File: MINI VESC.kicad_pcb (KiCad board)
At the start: 4 copper layers, 65 x 18 mm, 151 parts, among them P1 CONN_1, P10 CONN_01X06, P11 CONN_01X06, P2 CONN_1, P3 CONN_1, P4 CONN_1, P5 CONN_1, P6 CONN_1, P9 CONN_01X06, Q1 Q_NMOS_GSD, Q2 Q_NMOS_GSD, Q3 Q_NMOS_GSD, Q4 Q_NMOS_GSD, Q5 Q_NMOS_GSD, Q6 Q_NMOS_GSD, U1 LM5113, U10 MCP1700, U2 LM5113, U3 LM5113, U4 AD8418, U5 AD8418, U6 AD8418, U7 STM32F40X_LQFP64, U8 LMR16006, U9 MCP1700, X1 CRYSTAL_SMD

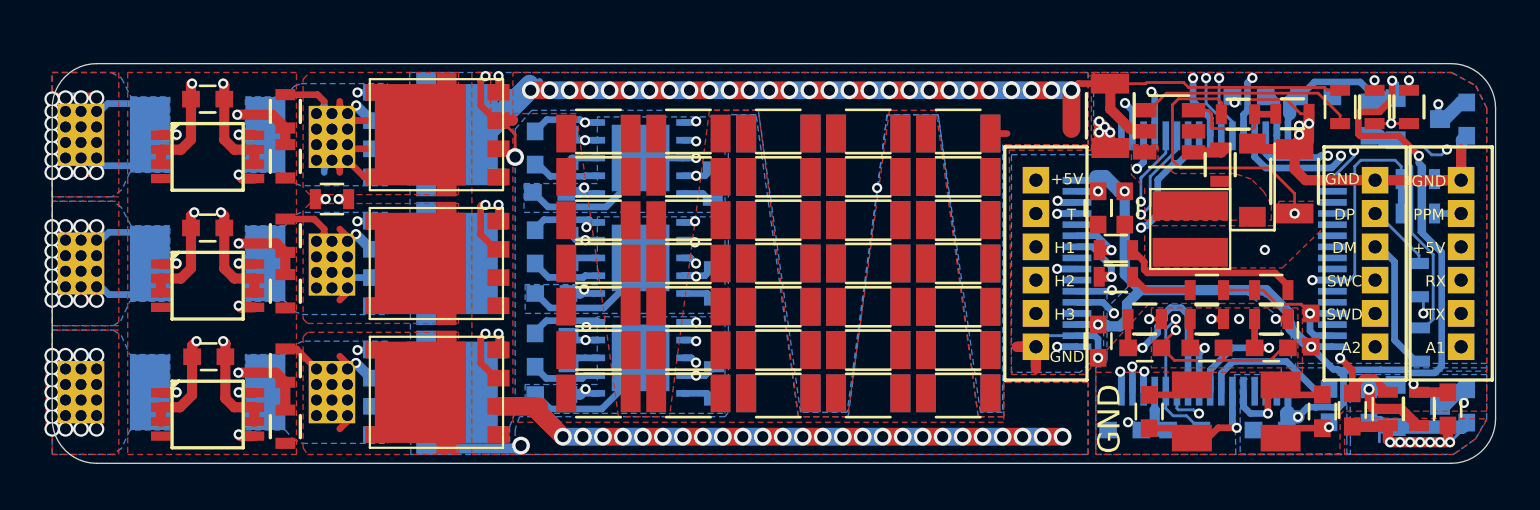
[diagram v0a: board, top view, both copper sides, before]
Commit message: Migrating to KiCAD 7
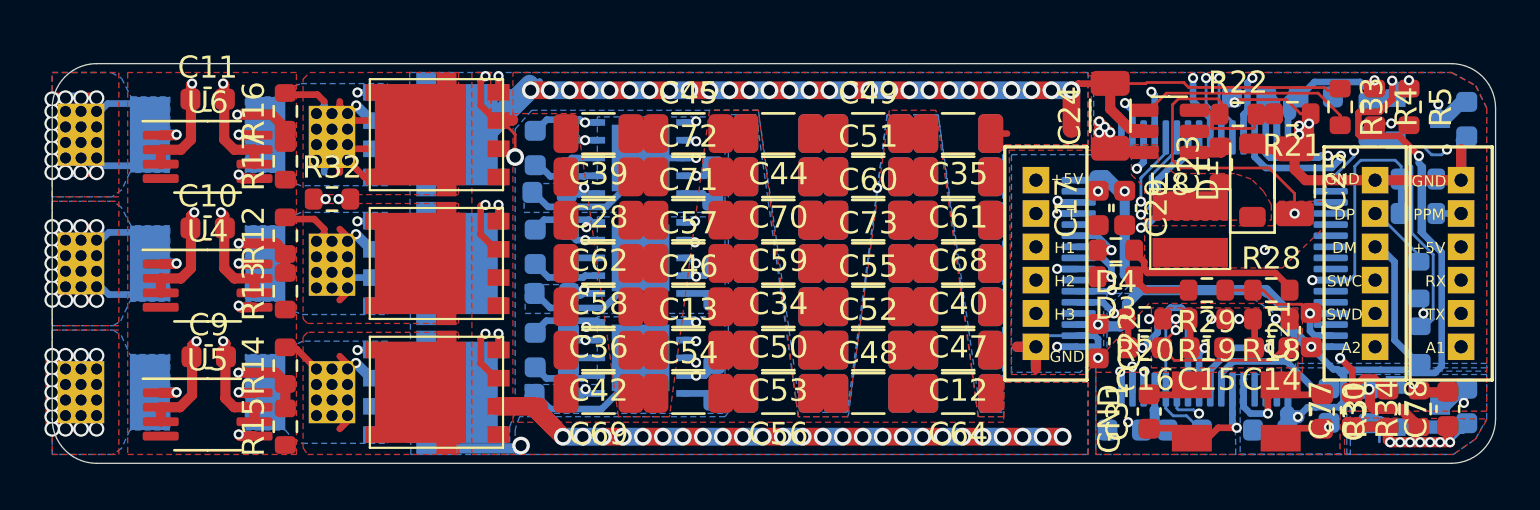
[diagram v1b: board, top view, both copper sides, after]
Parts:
- C1, C10, C11, C14, C15, C16, C17, C18, C19, C2, C20, C21, C22, C26, C27, C29, C3, C30, C31, C6, C7, C77, C78, C8, C86, C87, C88, C89, C9, C90: footprint Capacitors_SMD:C_0603 -> Capacitor_SMD:C_0603_1608Metric
- C12, C13, C24, C25, C28, C32, C33, C34, C35, C36, C37, C38, C39, C4, C40, C41, C42, C43, C44, C45, C46, C47, C48, C49, C5, C50, C51, C52, C53, C54, C55, C56, C57, C58, C59, C60, C61, C62, C63, C64, C65, C66, C67, C68, C69, C70, C71, C72, C73, C74, C75, C79, C80, C81, C82, C83, C84, C85: footprint Resistors_SMD:R_1206 -> Resistor_SMD:R_1206_3216Metric
- C23, C76, D3, D4, R10, R11, R12, R13, R14, R15, R16, R17, R18, R19, R20, R21, R22, R25, R27, R28, R29, R30, R31, R32, R33, R34, R4, R5, R6, R7, R8, R9: footprint Resistors_SMD:R_0603 -> Resistor_SMD:R_0603_1608Metric
- D1: footprint Diodes_SMD:D_SOD-123 -> Diode_SMD:D_SOD-123
- U4, U5, U6: footprint kicad_subory:MSOP -> Package_SO:MSOP-8_3x3mm_P0.65mm
- U7: footprint crf1:lqfp64_pad_mod -> Package_QFP:LQFP-64_10x10mm_P0.5mm
- U8: footprint TO_SOT_Packages_SMD:SOT-23-6 -> Package_TO_SOT_SMD:SOT-23-6
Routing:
- net VSS: track 317.9 -> 335.3 mm
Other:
- net class Default removed

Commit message: Lots of stuff
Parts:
- C1, C2, C3: value 220n -> 470n
- C12, C13, C25, C28, C32, C33, C34, C35, C36, C37, C38, C39, C4, C40, C41, C42, C43, C44, C45, C46, C47, C48, C49, C5, C50, C51, C52, C53, C54, C55, C56, C57, C58, C59, C60, C61, C62, C63, C64, C65, C66, C67, C68, C69, C70, C71, C72, C73, C74, C75, C79, C81, C82, C83, C84, C85: footprint Resistor_SMD:R_1206_3216Metric -> Capacitor_SMD:C_1206_3216Metric
- C19, C21, C22, C26, C27, C29: value 2u2 -> 100n
- C20: value 220nF -> 100n
- C23, C76: footprint Resistor_SMD:R_0603_1608Metric -> Capacitor_SMD:C_0603_1608Metric
- C24: value 10u -> 2u2; footprint Resistor_SMD:R_1206_3216Metric -> Capacitor_SMD:C_1206_3216Metric
- C80: value C -> 10u; footprint Resistor_SMD:R_1206_3216Metric -> Capacitor_SMD:C_1206_3216Metric
- D3, D4: footprint Resistor_SMD:R_0603_1608Metric -> LED_SMD:LED_0603_1608Metric
- L1: value 22uH -> Wurth Electronics 74438335220
- Q1, Q2, Q3, Q4, Q5, Q6: value Q_NMOS_GSD -> NTMFS5C604NLT1G
- R1, R2, R3: value RSENS -> R0005
- R10, R11, R6, R7, R8, R9: value 7R5 -> 3R9
- R12, R14, R4: value 25k5 -> 39k
- R21: value 510R -> 10k
- R22: value 8k -> 54k9
- R33: value 10k -> 100k
- X1: value CRYSTAL_SMD -> ABM3B-8.000MHZ
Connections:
- C1 pad 1: Net-(C1-Pad1) -> Net-(U1-HB)
- C17 pad 2: Net-(C17-Pad2) -> Net-(U7-VCAP1)
- C18 pad 2: Net-(C18-Pad2) -> Net-(U7-VCAP2)
- C2 pad 1: Net-(C2-Pad1) -> Net-(U2-HB)
- C20 pad 2: Net-(C20-Pad2) -> Net-(U7-NRST)
- C23 pad 1: Net-(C23-Pad1) -> Net-(D1-K)
- C23 pad 2: Net-(C23-Pad2) -> Net-(U8-BST)
- C3 pad 1: Net-(C3-Pad1) -> Net-(U3-HB)
- C30 pad 1: Net-(C30-Pad1) -> Net-(U7-PH0-OSC_IN)
- C31 pad 1: Net-(C31-Pad1) -> Net-(U7-PH1-OSC_OUT)
- C77 pad 2: Net-(C77-Pad2) -> Net-(U7-PA3(ADC123_IN3))
- L1 pad 1: Net-(C23-Pad1) -> Net-(D1-K)
- P1 pad 1: Net-(P1-Pad1) -> Net-(U4-IN-)
- P2 pad 1: Net-(P2-Pad1) -> Net-(U5-IN-)
- P3 pad 1: Net-(P3-Pad1) -> Net-(U6-IN-)
- Q1 pad 1: Net-(Q1-Pad1) -> Net-(Q1-G)
- Q2 pad 1: Net-(Q2-Pad1) -> Net-(Q2-G)
- Q3 pad 1: Net-(Q3-Pad1) -> Net-(Q3-G)
- Q4 pad 1: Net-(Q4-Pad1) -> Net-(Q4-G)
- Q5 pad 1: Net-(Q5-Pad1) -> Net-(Q5-G)
- Q6 pad 1: Net-(Q6-Pad1) -> Net-(Q6-G)
- R1 pad 1: Net-(P1-Pad1) -> Net-(U4-IN-)
- R10 pad 1: Net-(Q5-Pad1) -> Net-(Q5-G)
- R10 pad 2: Net-(R10-Pad2) -> Net-(U3-HO)
- R11 pad 1: Net-(R11-Pad1) -> Net-(U3-LO)
- R11 pad 2: Net-(Q6-Pad1) -> Net-(Q6-G)
- R2 pad 1: Net-(P2-Pad1) -> Net-(U5-IN-)
- R21 pad 2: Net-(R21-Pad2) -> Net-(U8-FB)
- R22 pad 2: Net-(R21-Pad2) -> Net-(U8-FB)
- R3 pad 1: Net-(P3-Pad1) -> Net-(U6-IN-)
- R31 pad 2: Net-(C77-Pad2) -> Net-(U7-PA3(ADC123_IN3))
- R32 pad 2: Net-(C77-Pad2) -> Net-(U7-PA3(ADC123_IN3))
- R6 pad 1: Net-(Q1-Pad1) -> Net-(Q1-G)
- R6 pad 2: Net-(R6-Pad2) -> Net-(U1-HO)
- R7 pad 1: Net-(R7-Pad1) -> Net-(U1-LO)
- R7 pad 2: Net-(Q2-Pad1) -> Net-(Q2-G)
- R8 pad 1: Net-(Q3-Pad1) -> Net-(Q3-G)
- R8 pad 2: Net-(R8-Pad2) -> Net-(U2-HO)
- R9 pad 1: Net-(R9-Pad1) -> Net-(U2-LO)
- R9 pad 2: Net-(Q4-Pad1) -> Net-(Q4-G)
- X1 pad 1: Net-(C30-Pad1) -> Net-(U7-PH0-OSC_IN)
- X1 pad 2: Net-(C31-Pad1) -> Net-(U7-PH1-OSC_OUT)
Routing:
- net VDD: track 123.7 -> 105.7 mm
- net VSS: track 335.3 -> 321.1 mm
- net Net-(U5-IN-): track 0.00 -> 11.5 mm, vias 0 -> 13
- net Net-(P2-Pad1): track 13.4 -> 1.92 mm, vias 14 -> 1
- net Net-(D4-Pad1): track 0.00 -> 8.12 mm
- net Net-(D4-K): track 8.12 -> 0.00 mm
- net ADC_EXT2: track 15.3 -> 21.9 mm, vias 1 -> 2
- net Net-(C31-Pad1): track 6.65 -> 0.00 mm, vias 1 -> 0
- net ADC_EXT1: track 35.3 -> 41.7 mm, vias 2 -> 3
- net Net-(C30-Pad1): track 6.43 -> 0.00 mm, vias 1 -> 0
- net Net-(U7-Pad23): track 0.00 -> 6.38 mm
- net Net-(C20-Pad2): track 6.38 -> 0.00 mm
- net Net-(P10-Pin_4): track 6.22 -> 0.00 mm
- net (no net): track 0.00 -> 6.22 mm
- net VCC: track 86.4 -> 82.9 mm
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- added copper zone on F.Cu, net Net-(D1-K)
- added copper zone on B.Cu, net Net-(U4-IN-)
- added copper zone on F.Cu, net Net-(U4-IN-)
- added copper zone on In1.Cu, net Net-(U4-IN-)
- added copper zone on In2.Cu, net Net-(U4-IN-)
- added copper zone on B.Cu, net Net-(U5-IN-)
- added copper zone on F.Cu, net Net-(U5-IN-)
- added copper zone on In1.Cu, net Net-(U5-IN-)
- added copper zone on In2.Cu, net Net-(U5-IN-)
- added copper zone on B.Cu, net Net-(U6-IN-)
- added copper zone on F.Cu, net Net-(U6-IN-)
- added copper zone on In1.Cu, net Net-(U6-IN-)
- added copper zone on In2.Cu, net Net-(U6-IN-)
- removed copper zone on F.Cu, net Net-(C23-Pad1)
- removed copper zone on B.Cu, net Net-(P1-Pad1)
- removed copper zone on F.Cu, net Net-(P1-Pad1)
- removed copper zone on In1.Cu, net Net-(P1-Pad1)
- removed copper zone on In2.Cu, net Net-(P1-Pad1)
- removed copper zone on B.Cu, net Net-(P2-Pad1)
- removed copper zone on F.Cu, net Net-(P2-Pad1)
- removed copper zone on In1.Cu, net Net-(P2-Pad1)
- removed copper zone on In2.Cu, net Net-(P2-Pad1)
- removed copper zone on B.Cu, net Net-(P3-Pad1)
- removed copper zone on F.Cu, net Net-(P3-Pad1)
- removed copper zone on In1.Cu, net Net-(P3-Pad1)
- removed copper zone on In2.Cu, net Net-(P3-Pad1)

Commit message: More work
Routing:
- net VSS: track 321.1 -> 298.6 mm
- net VDD: track 105.7 -> 93.0 mm
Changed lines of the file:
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@@
   (segment (start 132.52 85.07) (end 130.85 83.4) (width 0.127) (layer "In1.Cu") (net 1))
   (segment (start 88.2825 83.295) (end 89.455 83.295) (width 0.3) (layer "B.Cu") (net 1))
-  (segment (start 92.2 83.2) (end 93.1 83.2) (width 0.8) (layer "B.Cu") (net 1))
-  (segment (start 90.4 83.2) (end 91.3 83.2) (width 0.8) (layer "B.Cu") (net 1))
-  (segment (start 97.6 83.2) (end 98.5 83.2) (width 0.8) (layer "B.Cu") (net 1))
   (segment (start 84.8425 99.3275) (end 88.985466 99.3275) (width 0.46) (layer "B.Cu") (net 1))
-  (segment (start 104.8 83.2) (end 105.7 83.2) (width 0.8) (layer "B.Cu") (net 1))
   (segment (start 86.0175 85.2) (end 87.55 85.2) (width 0.8) (layer "B.Cu") (net 1))
   (segment (start 89.455 83.295) (end 89.55 83.2) (width 0.3) (layer "B.Cu") (net 1))
-  (segment (start 108.4 83.2) (end 109.3 83.2) (width 0.8) (layer "B.Cu") (net 1))
-  (segment (start 94 83.2) (end 94.9 83.2) (width 0.8) (layer "B.Cu") (net 1))
   (segment (start 88.985466 99.3275) (end 89.113216 99.19975) (width 0.46) (layer "B.Cu") (net 1))
-  (segment (start 113 83.2) (end 113.9 83.2) (width 0.8) (layer "B.Cu") (net 1))
-  (segment (start 101.2 83.2) (end 102.1 83.2) (width 0.8) (layer "B.Cu") (net 1))
   (segment (start 87.55 85.2) (end 89.55 83.2) (width 0.8) (layer "B.Cu") (net 1))
-  (segment (start 99.4 83.2) (end 100.3 83.2) (width 0.8) (layer "B.Cu") (net 1))
-  (segment (start 95.8 83.2) (end 96.7 83.2) (width 0.8) (layer "B.Cu") (net 1))
   (segment (start 86.0175 85.2) (end 87.2 85.2) (width 0.8) (layer "B.Cu") (net 1))
-  (segment (start 110.2 83.2) (end 111.2 83.2) (width 0.8) (layer "B.Cu") (net 1))
   (segment (start 86.0175 96.8) (end 87.177002 96.8) (width 0.46) (layer "B.Cu") (net 1))
-  (segment (start 103 83.2) (end 103.9 83.2) (width 0.8) (layer "B.Cu") (net 1))
-  (segment (start 106.6 83.2) (end 107.5 83.2) (width 0.8) (layer "B.Cu") (net 1))
-  (segment (start 111.2 83.2) (end 112.1 83.2) (width 0.8) (layer "B.Cu") (net 1))
   (segment (start 81.746359 89.096639) (end 81.742998 89.1) (width 0.46) (layer "In1.Cu") (net 2))
   (segment (start 81.742998 89.1) (end 82.068267 89.1) (width 0.46) (layer "In2.Cu") (net 2))
@@
   (segment (start 90.427001 93.002001) (end 92.847999 93.002001) (width 0.3) (layer "B.Cu") (net 4))
   (segment (start 89.75 96.9) (end 89.775 96.9) (width 0.3) (layer "B.Cu") (net 4))
-  (segment (start 106.3 98.8) (end 107.2 98.8) (width 0.8) (layer "B.Cu") (net 4))
-  (segment (start 112.6 98.8) (end 113.5 98.8) (width 0.8) (layer "B.Cu") (net 4))
   (segment (start 92.946601 88.452001) (end 94.5 86.898602) (width 0.3) (layer "B.Cu") (net 4))
   (segment (start 92.747999 97.552001) (end 94.5 95.8) (width 0.3) (layer "B.Cu") (net 4))
@@
   (segment (start 118.14994 96.75056) (end 118.14994 97.5278) (width 0.127) (layer "B.Cu") (net 4))
   (segment (start 115.1 94.400758) (end 114.950442 94.2512) (width 0.3) (layer "B.Cu") (net 4))
-  (segment (start 102.7 98.8) (end 103.6 98.8) (width 0.8) (layer "B.Cu") (net 4))
   (segment (start 92.847999 93.002001) (end 94.5 91.35) (width 0.3) (layer "B.Cu") (net 4))
   (segment (start 94.5 91.35) (end 94.5 90.75) (width 0.3) (layer "B.Cu") (net 4))
-  (segment (start 109 98.8) (end 109.9 98.8) (width 0.8) (layer "B.Cu") (net 4))
   (segment (start 131.45 85.5) (end 131.7 85.25) (width 0.46) (layer "B.Cu") (net 4))
   (segment (start 118.48214 97.86) (end 119.085 97.86) (width 0.127) (layer "B.Cu") (net 4))
-  (segment (start 109.9 98.8) (end 110.8 98.8) (width 0.8) (layer "B.Cu") (net 4))
-  (segment (start 97.3 98.8) (end 98.2 98.8) (width 0.8) (layer "B.Cu") (net 4))
   (segment (start 127.95 85.45) (end 128.5 85.45) (width 0.6) (layer "B.Cu") (net 4))
-  (segment (start 110.8 98.8) (end 111.7 98.8) (width 0.8) (layer "B.Cu") (net 4))
-  (segment (start 111.7 98.8) (end 112.6 98.8) (width 0.8) (layer "B.Cu") (net 4))
-  (segment (start 103.6 98.8) (end 104.5 98.8) (width 0.8) (layer "B.Cu") (net 4))
   (segment (start 115.1 95.25) (end 115.1 94.400758) (width 0.3) (layer "B.Cu") (net 4))
-  (segment (start 98.2 98.8) (end 99.1 98.8) (width 0.8) (layer "B.Cu") (net 4))
   (segment (start 94.5 95.8) (end 94.5 95.25) (width 0.3) (layer "B.Cu") (net 4))
   (segment (start 127.3 98.167242) (end 127.767242 98.167242) (width 0.6) (layer "B.Cu") (net 4))
   (segment (start 131.5 98.367242) (end 128.5 98.367242) (width 0.6) (layer "B.Cu") (net 4))
-  (segment (start 100 98.8) (end 100.9 98.8) (width 0.8) (layer "B.Cu") (net 4))
   (segment (start 89.65 87.8) (end 89.675 87.8) (width 0.3) (layer "B.Cu") (net 4))
   (segment (start 89.675 87.8) (end 90.327001 88.452001) (width 0.3) (layer "B.Cu") (net 4))
   (segment (start 114.14944 94.2512) (end 112.7988 94.2512) (width 0.127) (layer "B.Cu") (net 4))
-  (segment (start 91 98.8) (end 91.9 98.8) (width 0.8) (layer "B.Cu") (net 4))
-  (segment (start 92.8 98.8) (end 93.7 98.8) (width 0.8) (layer "B.Cu") (net 4))
   (segment (start 96.4 90.75) (end 96.742998 90.75) (width 0.3) (layer "B.Cu") (net 4))
   (segment (start 127.767242 98.167242) (end 127.967242 98.367242) (width 0.6) (layer "B.Cu") (net 4))
-  (segment (start 96.4 98.8) (end 97.3 98.8) (width 0.8) (layer "B.Cu") (net 4))
   (segment (start 114.950442 94.2512) (end 114.14944 94.2512) (width 0.3) (layer "B.Cu") (net 4))
   (segment (start 119.725 98.5) (end 119.75 98.5) (width 0.127) (layer "B.Cu") (net 4))
   (segment (start 96.4 86.25) (end 96.995124 86.25) (width 0.3) (layer "B.Cu") (net 4))
-  (segment (start 101.8 98.8) (end 102.7 98.8) (width 0.8) (layer "B.Cu") (net 4))
-  (segment (start 105.4 98.8) (end 106.3 98.8) (width 0.8) (layer "B.Cu") (net 4))
   (segment (start 128.7 99.05) (end 128.25 99.05) (width 0.127) (layer "B.Cu") (net 4))
   (segment (start 131.45 87.25) (end 131.45 85.5) (width 0.46) (layer "B.Cu") (net 4))
@@
   (segment (start 89.775 96.9) (end 90.427001 97.552001) (width 0.3) (layer "B.Cu") (net 4))
   (segment (start 121.15 83.5) (end 121.15 83.643987) (width 0.127) (layer "B.Cu") (net 4))
-  (segment (start 94.6 98.8) (end 95.5 98.8) (width 0.8) (layer "B.Cu") (net 4))
   (segment (start 124.852098 94.2512) (end 125.65056 94.2512) (width 0.3) (layer "B.Cu") (net 4))
-  (segment (start 99.1 98.8) (end 100 98.8) (width 0.8) (layer "B.Cu") (net 4))
   (segment (start 118.14994 96.75056) (end 118.14994 93.950059) (width 0.127) (layer "B.Cu") (net 4))
   (segment (start 129.6 99.05) (end 129.15 99.05) (width 0.127) (layer "B.Cu") (net 4))
   (segment (start 127.3 85.25) (end 127.75 85.25) (width 0.6) (layer "B.Cu") (net 4))
-  (segment (start 93.7 98.8) (end 94.6 98.8) (width 0.8) (layer "B.Cu") (net 4))
   (segment (start 131.45 87.25) (end 130.3 87.25) (width 0.46) (layer "B.Cu") (net 4))
   (segment (start 118.14994 93.950059) (end 118.6 93.499999) (width 0.127) (layer "B.Cu") (net 4))
@@
   (segment (start 118.14994 97.5278) (end 118.48214 97.86) (width 0.127) (layer "B.Cu") (net 4))
   (segment (start 115.154009 84.604009) (end 115.4 84.85) (width 0.127) (layer "B.Cu") (net 4))
-  (segment (start 107.2 98.8) (end 108.1 98.8) (width 0.8) (layer "B.Cu") (net 4))
-  (segment (start 95.5 98.8) (end 96.4 98.8) (width 0.8) (layer "B.Cu") (net 4))
   (segment (start 112.7988 94.2512) (end 112.3 94.75) (width 0.127) (layer "B.Cu") (net 4))
   (segment (start 131.7 98.167242) (end 131.7 98.3) (width 0.127) (layer "B.Cu") (net 4))
   (segment (start 96.995124 86.25) (end 96.997562 86.247562) (width 0.3) (layer "B.Cu") (net 4))
-  (segment (start 100.9 98.8) (end 101.8 98.8) (width 0.8) (layer "B.Cu") (net 4))
   (segment (start 124.643318 93.25) (end 124.643318 94.04242) (width 0.3) (layer "B.Cu") (net 4))
   (segment (start 130.3 87.25) (end 130.25 87.2) (width 0.46) (layer "B.Cu") (net 4))
-  (segment (start 108.1 98.8) (end 109 98.8) (width 0.8) (layer "B.Cu") (net 4))
   (segment (start 96.4 95.25) (end 96.779887 95.25) (width 0.3) (layer "B.Cu") (net 4))
   (segment (start 115.15 84.604009) (end 115.154009 84.604009) (width 0.127) (layer "B.Cu") (net 4))
-  (segment (start 91.9 98.8) (end 92.8 98.8) (width 0.8) (layer "B.Cu") (net 4))
-  (segment (start 104.5 98.8) (end 105.4 98.8) (width 0.8) (layer "B.Cu") (net 4))
   (segment (start 96.4 86.25) (end 94.5 86.25) (width 0.3) (layer "B.Cu") (net 4))
   (segment (start 127.967242 98.367242) (end 128.5 98.367242) (width 0.6) (layer "B.Cu") (net 4))
